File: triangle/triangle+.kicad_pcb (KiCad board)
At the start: 2 copper layers, 50 x 43.2 mm, 11 parts, among them J1 Conn_01x05_Pin, J2 Conn_01x05_Pin, J3 Conn_01x05_Pin

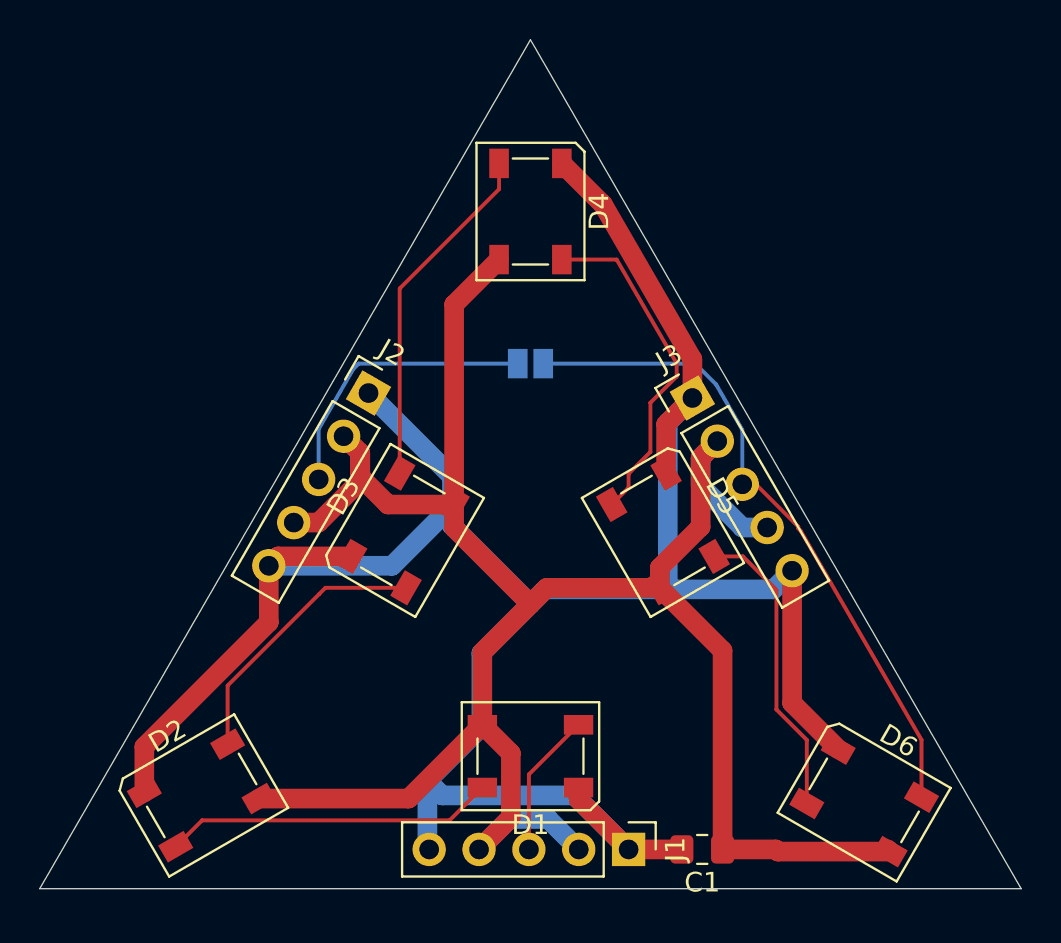
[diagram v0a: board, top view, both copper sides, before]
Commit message: added mic to antenna, decagons, octagons and all the shenanigans
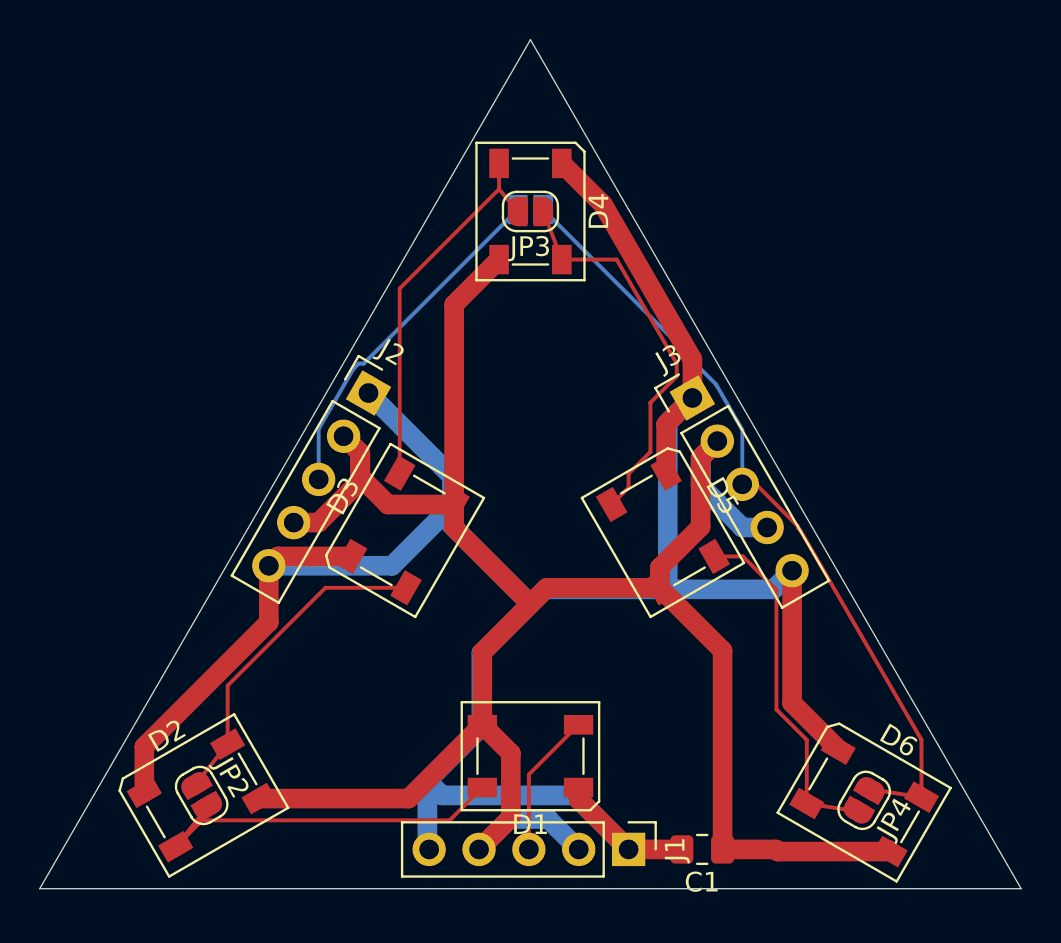
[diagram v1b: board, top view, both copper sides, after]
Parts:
- added JP2: SolderJumper_2_Open, Jumper:SolderJumper-2_P1.3mm_Open_RoundedPad1.0x1.5mm, F.Cu at (83.2, 95.2)
- added JP3: SolderJumper_2_Open, Jumper:SolderJumper-2_P1.3mm_Open_RoundedPad1.0x1.5mm, F.Cu at (100.0, 65.5)
- added JP4: SolderJumper_2_Open, Jumper:SolderJumper-2_P1.3mm_Open_RoundedPad1.0x1.5mm, F.Cu at (117.0, 95.5)
- moved JP1 7.85 mm to (100.0, 65.4)
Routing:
- net Net-(D6-DOUT): track 33.9 -> 39.9 mm
- net Net-(J2-Pin_3): track 14.6 -> 17.8 mm
- net Net-(D4-DOUT): track 17.5 -> 20.1 mm
- net Net-(D5-DOUT): track 15.4 -> 18.0 mm
- net Net-(D2-DOUT): track 14.1 -> 16.8 mm
- net Net-(D1-DOUT): track 16.9 -> 19.5 mm
- net Net-(D3-DOUT): track 17.9 -> 19.4 mm
